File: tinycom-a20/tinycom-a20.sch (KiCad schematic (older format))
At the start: 36 parts, among them P1 CONN_02X08, P2 CONN_02X08, U1 ALLWINNERA10/TFBGA441, U2 H5TQG63BFR/FBGA96, U3 H27UBG8T2A/TSOP48, Y1 Crystal_Small, Y2 Crystal_Small

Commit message: add power routes
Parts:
- gave numbers to parts that had none: 2
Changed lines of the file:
@@
 $EndComp
 $Comp
-L GND #PWR01
+L GND #PWR21
 U 1 1 563E445F
 P 17800 6150
-F 0 "#PWR01" H 17800 5900 50  0001 C CNN
+F 0 "#PWR21" H 17800 5900 50  0001 C CNN
 F 1 "GND" H 17800 6000 50  0000 C CNN
 F 2 "" H 17800 6150 60  0000 C CNN
@@
 SCK_P
 $Comp
-L GND #PWR02
+L GND #PWR19
 U 1 1 563ECE56
 P 14950 850
-F 0 "#PWR02" H 14950 600 50  0001 C CNN
+F 0 "#PWR19" H 14950 600 50  0001 C CNN
 F 1 "GND" H 14950 700 50  0000 C CNN
 F 2 "" H 14950 850 60  0000 C CNN
@@
 $EndComp
 $Comp
-L GND #PWR03
+L GND #PWR17
 U 1 1 563EDF36
 P 13600 5900
-F 0 "#PWR03" H 13600 5650 50  0001 C CNN
+F 0 "#PWR17" H 13600 5650 50  0001 C CNN
 F 1 "GND" H 13600 5750 50  0000 C CNN
 F 2 "" H 13600 5900 60  0000 C CNN
@@
 $EndComp
 $Comp
-L GND #PWR04
+L GND #PWR18
 U 1 1 563EE398
 P 14350 5150
-F 0 "#PWR04" H 14350 4900 50  0001 C CNN
+F 0 "#PWR18" H 14350 4900 50  0001 C CNN
 F 1 "GND" H 14350 5000 50  0000 C CNN
 F 2 "" H 14350 5150 60  0000 C CNN
@@
 $EndComp
 $Comp
-L GND #PWR05
+L GND #PWR10
 U 1 1 56400687
 P 12400 9950
-F 0 "#PWR05" H 12400 9700 50  0001 C CNN
+F 0 "#PWR10" H 12400 9700 50  0001 C CNN
 F 1 "GND" H 12400 9800 50  0000 C CNN
 F 2 "" H 12400 9950 60  0000 C CNN
@@
 $EndComp
 $Comp
-L GND #PWR06
+L GND #PWR11
 U 1 1 56400704
 P 12650 9950
-F 0 "#PWR06" H 12650 9700 50  0001 C CNN
+F 0 "#PWR11" H 12650 9700 50  0001 C CNN
 F 1 "GND" H 12650 9800 50  0000 C CNN
 F 2 "" H 12650 9950 60  0000 C CNN
@@
 $EndComp
 $Comp
-L GND #PWR07
+L GND #PWR9
 U 1 1 56408532
 P 12150 9250
-F 0 "#PWR07" H 12150 9000 50  0001 C CNN
+F 0 "#PWR9" H 12150 9000 50  0001 C CNN
 F 1 "GND" H 12150 9100 50  0000 C CNN
 F 2 "" H 12150 9250 60  0000 C CNN
@@
 $EndComp
 $Comp
-L GND #PWR08
+L GND #PWR12
 U 1 1 56408573
 P 12700 9300
-F 0 "#PWR08" H 12700 9050 50  0001 C CNN
+F 0 "#PWR12" H 12700 9050 50  0001 C CNN
 F 1 "GND" H 12700 9150 50  0000 C CNN
 F 2 "" H 12700 9300 60  0000 C CNN
@@
 $EndComp
 $Comp
-L GND #PWR09
+L GND #PWR14
 U 1 1 5640D8CA
 P 12750 6950
-F 0 "#PWR09" H 12750 6700 50  0001 C CNN
+F 0 "#PWR14" H 12750 6700 50  0001 C CNN
 F 1 "GND" H 12750 6800 50  0000 C CNN
 F 2 "" H 12750 6950 60  0000 C CNN
@@
 $EndComp
 $Comp
-L GND #PWR010
+L GND #PWR24
 U 1 1 56408FCA
 P 19800 9350
-F 0 "#PWR010" H 19800 9100 50  0001 C CNN
+F 0 "#PWR24" H 19800 9100 50  0001 C CNN
 F 1 "GND" H 19800 9200 50  0000 C CNN
 F 2 "" H 19800 9350 60  0000 C CNN
@@
 UDP2
 $Comp
-L GND #PWR011
+L GND #PWR26
 U 1 1 56411561
 P 20650 10200
-F 0 "#PWR011" H 20650 9950 50  0001 C CNN
+F 0 "#PWR26" H 20650 9950 50  0001 C CNN
 F 1 "GND" H 20650 10050 50  0000 C CNN
 F 2 "" H 20650 10200 60  0000 C CNN
@@
 NoConn ~ 7500 2750
 $Comp
-L GND #PWR012
+L GND #PWR8
 U 1 1 56414A5D
 P 8850 1300
-F 0 "#PWR012" H 8850 1050 50  0001 C CNN
+F 0 "#PWR8" H 8850 1050 50  0001 C CNN
 F 1 "GND" H 8850 1150 50  0000 C CNN
 F 2 "" H 8850 1300 60  0000 C CNN
@@
 VCC_15
 $Comp
-L GND #PWR013
+L GND #PWR1
 U 1 1 56417328
 P 800 9350
-F 0 "#PWR013" H 800 9100 50  0001 C CNN
+F 0 "#PWR1" H 800 9100 50  0001 C CNN
 F 1 "GND" H 800 9200 50  0000 C CNN
 F 2 "" H 800 9350 60  0000 C CNN
@@
 NoConn ~ 1050 13300
 $Comp
-L GND #PWR014
+L GND #PWR3
 U 1 1 56417B02
 P 900 13450
-F 0 "#PWR014" H 900 13200 50  0001 C CNN
+F 0 "#PWR3" H 900 13200 50  0001 C CNN
 F 1 "GND" H 900 13300 50  0000 C CNN
 F 2 "" H 900 13450 60  0000 C CNN
@@
 NoConn ~ 1050 13700
 $Comp
-L GND #PWR015
+L GND #PWR2
 U 1 1 56417F5A
 P 850 13800
-F 0 "#PWR015" H 850 13550 50  0001 C CNN
+F 0 "#PWR2" H 850 13550 50  0001 C CNN
 F 1 "GND" H 850 13650 50  0000 C CNN
 F 2 "" H 850 13800 60  0000 C CNN
@@
 NoConn ~ 5650 11400
 $Comp
-L GND #PWR016
+L GND #PWR6
 U 1 1 56418E41
 P 5850 12050
-F 0 "#PWR016" H 5850 11800 50  0001 C CNN
+F 0 "#PWR6" H 5850 11800 50  0001 C CNN
 F 1 "GND" H 5850 11900 50  0000 C CNN
 F 2 "" H 5850 12050 60  0000 C CNN
@@
 $EndComp
 $Comp
-L GND #PWR017
+L GND #PWR7
 U 1 1 56419222
 P 5900 12300
-F 0 "#PWR017" H 5900 12050 50  0001 C CNN
+F 0 "#PWR7" H 5900 12050 50  0001 C CNN
 F 1 "GND" H 5900 12150 50  0000 C CNN
 F 2 "" H 5900 12300 60  0000 C CNN
@@
 NoConn ~ 11650 14450
 $Comp
-L GND #PWR018
+L GND #PWR16
 U 1 1 5641B53D
 P 12900 9850
-F 0 "#PWR018" H 12900 9600 50  0001 C CNN
+F 0 "#PWR16" H 12900 9600 50  0001 C CNN
 F 1 "GND" H 12900 9700 50  0000 C CNN
 F 2 "" H 12900 9850 60  0000 C CNN
@@
 NoConn ~ 13000 10700
 $Comp
-L GND #PWR019
+L GND #PWR15
 U 1 1 5641BA06
 P 12850 11350
-F 0 "#PWR019" H 12850 11100 50  0001 C CNN
+F 0 "#PWR15" H 12850 11100 50  0001 C CNN
 F 1 "GND" H 12850 11200 50  0000 C CNN
 F 2 "" H 12850 11350 60  0000 C CNN
@@
 NoConn ~ 13000 12600
 $Comp
-L GND #PWR020
+L GND #PWR13
 U 1 1 5641C0BF
 P 12700 12700
-F 0 "#PWR020" H 12700 12450 50  0001 C CNN
+F 0 "#PWR13" H 12700 12450 50  0001 C CNN
 F 1 "GND" H 12700 12550 50  0000 C CNN
 F 2 "" H 12700 12700 60  0000 C CNN
@@
 $EndComp
 $Comp
-L GND #PWR021
+L GND #PWR20
 U 1 1 5641C64B
 P 17750 14500
-F 0 "#PWR021" H 17750 14250 50  0001 C CNN
+F 0 "#PWR20" H 17750 14250 50  0001 C CNN
 F 1 "GND" H 17750 14350 50  0000 C CNN
 F 2 "" H 17750 14500 60  0000 C CNN
@@
 $EndComp
 $Comp
-L GND #PWR022
+L GND #PWR22
 U 1 1 5641CC6D
 P 17800 13850
-F 0 "#PWR022" H 17800 13600 50  0001 C CNN
+F 0 "#PWR22" H 17800 13600 50  0001 C CNN
 F 1 "GND" H 17800 13700 50  0000 C CNN
 F 2 "" H 17800 13850 60  0000 C CNN
@@
 VCC_33
 $Comp
-L GND #PWR023
+L GND #PWR27
 U 1 1 5643044F
 P 20800 13600
-F 0 "#PWR023" H 20800 13350 50  0001 C CNN
+F 0 "#PWR27" H 20800 13350 50  0001 C CNN
 F 1 "GND" H 20800 13450 50  0000 C CNN
 F 2 "" H 20800 13600 60  0000 C CNN
@@
 VCC_33
 $Comp
-L GND #PWR024
+L GND #PWR5
 U 1 1 5643A4FE
 P 5850 10900
-F 0 "#PWR024" H 5850 10650 50  0001 C CNN
+F 0 "#PWR5" H 5850 10650 50  0001 C CNN
 F 1 "GND" H 5850 10750 50  0000 C CNN
 F 2 "" H 5850 10900 60  0000 C CNN
@@
 NoConn ~ 1050 14100
 $Comp
-L GND #PWR025
+L GND #PWR4
 U 1 1 5643BDD7
 P 950 11000
-F 0 "#PWR025" H 950 10750 50  0001 C CNN
+F 0 "#PWR4" H 950 10750 50  0001 C CNN
 F 1 "GND" H 950 10850 50  0000 C CNN
 F 2 "" H 950 11000 60  0000 C CNN
@@
 VCC_33
 $Comp
-L GND #PWR026
+L GND #PWR23
 U 1 1 56440C85
 P 19500 8700
-F 0 "#PWR026" H 19500 8450 50  0001 C CNN
+F 0 "#PWR23" H 19500 8450 50  0001 C CNN
 F 1 "GND" H 19500 8550 50  0000 C CNN
 F 2 "" H 19500 8700 60  0000 C CNN
@@
 $EndComp
 $Comp
-L GND #PWR027
+L GND #PWR25
 U 1 1 56441E51
 P 20300 8700
-F 0 "#PWR027" H 20300 8450 50  0001 C CNN
+F 0 "#PWR25" H 20300 8450 50  0001 C CNN
 F 1 "GND" H 20300 8550 50  0000 C CNN
 F 2 "" H 20300 8700 60  0000 C CNN
@@
 $EndComp
 $Comp
-L GND #PWR028
+L GND #PWR28
 U 1 1 564426D1
 P 20950 8700
-F 0 "#PWR028" H 20950 8450 50  0001 C CNN
+F 0 "#PWR28" H 20950 8450 50  0001 C CNN
 F 1 "GND" H 20950 8550 50  0000 C CNN
 F 2 "" H 20950 8700 60  0000 C CNN
@@
 $EndComp
 $Comp
-L C_Small C?
+L C_Small C13
 U 1 1 5645F6BF
 P 21550 8450
-F 0 "C?" H 21560 8520 50  0000 L CNN
+F 0 "C13" H 21560 8520 50  0000 L CNN
 F 1 "C_Small" H 21560 8370 50  0000 L CNN
 F 2 "Capacitors_SMD:C_0603" H 21550 8450 60  0001 C CNN
@@
 $EndComp
 $Comp
-L C_Small C?
+L C_Small C18
 U 1 1 5645F746
 P 21650 8450
-F 0 "C?" H 21660 8520 50  0000 L CNN
+F 0 "C18" H 21660 8520 50  0000 L CNN
 F 1 "C_Small" H 21660 8370 50  0000 L CNN
 F 2 "Capacitors_SMD:C_0603" H 21650 8450 60  0001 C CNN

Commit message: fix
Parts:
- added C? (x2): C_Small, Capacitors_SMD:C_0603, symbol C_Small
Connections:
- net GND: now also C?.2, C?.2
- net VCC_12: now also C?.1
- net VCC_33: now also C?.1
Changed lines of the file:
@@
 	19900 8600 19900 8550
 Wire Wire Line
-	19050 8300 19500 8300
+	19050 8300 19650 8300
 Wire Wire Line
-	19050 8600 19500 8600
+	19050 8600 19650 8600
 Wire Wire Line
 	20700 8550 21650 8550
@@
 Connection ~ 21400 8550
 Connection ~ 21550 8550
+$Comp
+L C_Small C?
+U 1 1 5647248A
+P 20000 8450
+F 0 "C?" H 20010 8520 50  0000 L CNN
+F 1 "C_Small" H 20010 8370 50  0000 L CNN
+F 2 "Capacitors_SMD:C_0603" H 20000 8450 60  0001 C CNN
+F 3 "" H 20000 8450 60  0000 C CNN
+	1    20000 8450
+	1    0    0    -1
+$EndComp
+Wire Wire Line
+	20000 8350 20000 8300
+Connection ~ 20000 8300
+Wire Wire Line
+	20000 8550 20000 8600
+Connection ~ 20000 8600
+$Comp
+L C_Small C?
+U 1 1 56472991
+P 19650 8450
+F 0 "C?" H 19660 8520 50  0000 L CNN
+F 1 "C_Small" H 19660 8370 50  0000 L CNN
+F 2 "Capacitors_SMD:C_0603" H 19650 8450 60  0001 C CNN
+F 3 "" H 19650 8450 60  0000 C CNN
+	1    19650 8450
+	1    0    0    -1
+$EndComp
+Wire Wire Line
+	19650 8300 19650 8350
+Wire Wire Line
+	19650 8600 19650 8550
 $EndSCHEMATC

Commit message: readme
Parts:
- gave numbers to parts that had none: 2
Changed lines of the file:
@@
 $EndComp
 $Comp
-L GND #PWR21
+L GND #PWR01
 U 1 1 563E445F
 P 17800 6150
-F 0 "#PWR21" H 17800 5900 50  0001 C CNN
+F 0 "#PWR01" H 17800 5900 50  0001 C CNN
 F 1 "GND" H 17800 6000 50  0000 C CNN
 F 2 "" H 17800 6150 60  0000 C CNN
@@
 SCK_P
 $Comp
-L GND #PWR19
+L GND #PWR02
 U 1 1 563ECE56
 P 14950 850
-F 0 "#PWR19" H 14950 600 50  0001 C CNN
+F 0 "#PWR02" H 14950 600 50  0001 C CNN
 F 1 "GND" H 14950 700 50  0000 C CNN
 F 2 "" H 14950 850 60  0000 C CNN
@@
 $EndComp
 $Comp
-L GND #PWR17
+L GND #PWR03
 U 1 1 563EDF36
 P 13600 5900
-F 0 "#PWR17" H 13600 5650 50  0001 C CNN
+F 0 "#PWR03" H 13600 5650 50  0001 C CNN
 F 1 "GND" H 13600 5750 50  0000 C CNN
 F 2 "" H 13600 5900 60  0000 C CNN
@@
 $EndComp
 $Comp
-L GND #PWR18
+L GND #PWR04
 U 1 1 563EE398
 P 14350 5150
-F 0 "#PWR18" H 14350 4900 50  0001 C CNN
+F 0 "#PWR04" H 14350 4900 50  0001 C CNN
 F 1 "GND" H 14350 5000 50  0000 C CNN
 F 2 "" H 14350 5150 60  0000 C CNN
@@
 $EndComp
 $Comp
-L GND #PWR10
+L GND #PWR05
 U 1 1 56400687
 P 12400 9950
-F 0 "#PWR10" H 12400 9700 50  0001 C CNN
+F 0 "#PWR05" H 12400 9700 50  0001 C CNN
 F 1 "GND" H 12400 9800 50  0000 C CNN
 F 2 "" H 12400 9950 60  0000 C CNN
@@
 $EndComp
 $Comp
-L GND #PWR11
+L GND #PWR06
 U 1 1 56400704
 P 12650 9950
-F 0 "#PWR11" H 12650 9700 50  0001 C CNN
+F 0 "#PWR06" H 12650 9700 50  0001 C CNN
 F 1 "GND" H 12650 9800 50  0000 C CNN
 F 2 "" H 12650 9950 60  0000 C CNN
@@
 $EndComp
 $Comp
-L GND #PWR9
+L GND #PWR07
 U 1 1 56408532
 P 12150 9250
-F 0 "#PWR9" H 12150 9000 50  0001 C CNN
+F 0 "#PWR07" H 12150 9000 50  0001 C CNN
 F 1 "GND" H 12150 9100 50  0000 C CNN
 F 2 "" H 12150 9250 60  0000 C CNN
@@
 $EndComp
 $Comp
-L GND #PWR12
+L GND #PWR08
 U 1 1 56408573
 P 12700 9300
-F 0 "#PWR12" H 12700 9050 50  0001 C CNN
+F 0 "#PWR08" H 12700 9050 50  0001 C CNN
 F 1 "GND" H 12700 9150 50  0000 C CNN
 F 2 "" H 12700 9300 60  0000 C CNN
@@
 $EndComp
 $Comp
-L GND #PWR14
+L GND #PWR09
 U 1 1 5640D8CA
 P 12750 6950
-F 0 "#PWR14" H 12750 6700 50  0001 C CNN
+F 0 "#PWR09" H 12750 6700 50  0001 C CNN
 F 1 "GND" H 12750 6800 50  0000 C CNN
 F 2 "" H 12750 6950 60  0000 C CNN
@@
 $EndComp
 $Comp
-L GND #PWR24
+L GND #PWR010
 U 1 1 56408FCA
 P 19800 9350
-F 0 "#PWR24" H 19800 9100 50  0001 C CNN
+F 0 "#PWR010" H 19800 9100 50  0001 C CNN
 F 1 "GND" H 19800 9200 50  0000 C CNN
 F 2 "" H 19800 9350 60  0000 C CNN
@@
 UDP2
 $Comp
-L GND #PWR26
+L GND #PWR011
 U 1 1 56411561
 P 20650 10200
-F 0 "#PWR26" H 20650 9950 50  0001 C CNN
+F 0 "#PWR011" H 20650 9950 50  0001 C CNN
 F 1 "GND" H 20650 10050 50  0000 C CNN
 F 2 "" H 20650 10200 60  0000 C CNN
@@
 NoConn ~ 7500 2750
 $Comp
-L GND #PWR8
+L GND #PWR012
 U 1 1 56414A5D
 P 8850 1300
-F 0 "#PWR8" H 8850 1050 50  0001 C CNN
+F 0 "#PWR012" H 8850 1050 50  0001 C CNN
 F 1 "GND" H 8850 1150 50  0000 C CNN
 F 2 "" H 8850 1300 60  0000 C CNN
@@
 VCC_15
 $Comp
-L GND #PWR1
+L GND #PWR013
 U 1 1 56417328
 P 800 9350
-F 0 "#PWR1" H 800 9100 50  0001 C CNN
+F 0 "#PWR013" H 800 9100 50  0001 C CNN
 F 1 "GND" H 800 9200 50  0000 C CNN
 F 2 "" H 800 9350 60  0000 C CNN
@@
 NoConn ~ 1050 13300
 $Comp
-L GND #PWR3
+L GND #PWR014
 U 1 1 56417B02
 P 900 13450
-F 0 "#PWR3" H 900 13200 50  0001 C CNN
+F 0 "#PWR014" H 900 13200 50  0001 C CNN
 F 1 "GND" H 900 13300 50  0000 C CNN
 F 2 "" H 900 13450 60  0000 C CNN
@@
 NoConn ~ 1050 13700
 $Comp
-L GND #PWR2
+L GND #PWR015
 U 1 1 56417F5A
 P 850 13800
-F 0 "#PWR2" H 850 13550 50  0001 C CNN
+F 0 "#PWR015" H 850 13550 50  0001 C CNN
 F 1 "GND" H 850 13650 50  0000 C CNN
 F 2 "" H 850 13800 60  0000 C CNN
@@
 NoConn ~ 5650 11400
 $Comp
-L GND #PWR6
+L GND #PWR016
 U 1 1 56418E41
 P 5850 12050
-F 0 "#PWR6" H 5850 11800 50  0001 C CNN
+F 0 "#PWR016" H 5850 11800 50  0001 C CNN
 F 1 "GND" H 5850 11900 50  0000 C CNN
 F 2 "" H 5850 12050 60  0000 C CNN
@@
 $EndComp
 $Comp
-L GND #PWR7
+L GND #PWR017
 U 1 1 56419222
 P 5900 12300
-F 0 "#PWR7" H 5900 12050 50  0001 C CNN
+F 0 "#PWR017" H 5900 12050 50  0001 C CNN
 F 1 "GND" H 5900 12150 50  0000 C CNN
 F 2 "" H 5900 12300 60  0000 C CNN
@@
 NoConn ~ 11650 14450
 $Comp
-L GND #PWR16
+L GND #PWR018
 U 1 1 5641B53D
 P 12900 9850
-F 0 "#PWR16" H 12900 9600 50  0001 C CNN
+F 0 "#PWR018" H 12900 9600 50  0001 C CNN
 F 1 "GND" H 12900 9700 50  0000 C CNN
 F 2 "" H 12900 9850 60  0000 C CNN
@@
 NoConn ~ 13000 10700
 $Comp
-L GND #PWR15
+L GND #PWR019
 U 1 1 5641BA06
 P 12850 11350
-F 0 "#PWR15" H 12850 11100 50  0001 C CNN
+F 0 "#PWR019" H 12850 11100 50  0001 C CNN
 F 1 "GND" H 12850 11200 50  0000 C CNN
 F 2 "" H 12850 11350 60  0000 C CNN
@@
 NoConn ~ 13000 12600
 $Comp
-L GND #PWR13
+L GND #PWR020
 U 1 1 5641C0BF
 P 12700 12700
-F 0 "#PWR13" H 12700 12450 50  0001 C CNN
+F 0 "#PWR020" H 12700 12450 50  0001 C CNN
 F 1 "GND" H 12700 12550 50  0000 C CNN
 F 2 "" H 12700 12700 60  0000 C CNN
@@
 $EndComp
 $Comp
-L GND #PWR20
+L GND #PWR021
 U 1 1 5641C64B
 P 17750 14500
-F 0 "#PWR20" H 17750 14250 50  0001 C CNN
+F 0 "#PWR021" H 17750 14250 50  0001 C CNN
 F 1 "GND" H 17750 14350 50  0000 C CNN
 F 2 "" H 17750 14500 60  0000 C CNN
@@
 $EndComp
 $Comp
-L GND #PWR22
+L GND #PWR022
 U 1 1 5641CC6D
 P 17800 13850
-F 0 "#PWR22" H 17800 13600 50  0001 C CNN
+F 0 "#PWR022" H 17800 13600 50  0001 C CNN
 F 1 "GND" H 17800 13700 50  0000 C CNN
 F 2 "" H 17800 13850 60  0000 C CNN
@@
 VCC_33
 $Comp
-L GND #PWR27
+L GND #PWR023
 U 1 1 5643044F
 P 20800 13600
-F 0 "#PWR27" H 20800 13350 50  0001 C CNN
+F 0 "#PWR023" H 20800 13350 50  0001 C CNN
 F 1 "GND" H 20800 13450 50  0000 C CNN
 F 2 "" H 20800 13600 60  0000 C CNN
@@
 VCC_33
 $Comp
-L GND #PWR5
+L GND #PWR024
 U 1 1 5643A4FE
 P 5850 10900
-F 0 "#PWR5" H 5850 10650 50  0001 C CNN
+F 0 "#PWR024" H 5850 10650 50  0001 C CNN
 F 1 "GND" H 5850 10750 50  0000 C CNN
 F 2 "" H 5850 10900 60  0000 C CNN
@@
 NoConn ~ 1050 14100
 $Comp
-L GND #PWR4
+L GND #PWR025
 U 1 1 5643BDD7
 P 950 11000
-F 0 "#PWR4" H 950 10750 50  0001 C CNN
+F 0 "#PWR025" H 950 10750 50  0001 C CNN
 F 1 "GND" H 950 10850 50  0000 C CNN
 F 2 "" H 950 11000 60  0000 C CNN
@@
 VCC_33
 $Comp
-L GND #PWR23
+L GND #PWR026
 U 1 1 56440C85
 P 19500 8700
-F 0 "#PWR23" H 19500 8450 50  0001 C CNN
+F 0 "#PWR026" H 19500 8450 50  0001 C CNN
 F 1 "GND" H 19500 8550 50  0000 C CNN
 F 2 "" H 19500 8700 60  0000 C CNN
@@
 $EndComp
 $Comp
-L GND #PWR25
+L GND #PWR027
 U 1 1 56441E51
 P 20300 8700
-F 0 "#PWR25" H 20300 8450 50  0001 C CNN
+F 0 "#PWR027" H 20300 8450 50  0001 C CNN
 F 1 "GND" H 20300 8550 50  0000 C CNN
 F 2 "" H 20300 8700 60  0000 C CNN
@@
 $EndComp
 $Comp
-L GND #PWR28
+L GND #PWR028
 U 1 1 564426D1
 P 20950 8700
-F 0 "#PWR28" H 20950 8450 50  0001 C CNN
+F 0 "#PWR028" H 20950 8450 50  0001 C CNN
 F 1 "GND" H 20950 8550 50  0000 C CNN
 F 2 "" H 20950 8700 60  0000 C CNN
@@
 Connection ~ 21550 8550
 $Comp
-L C_Small C?
+L C_Small C22
 U 1 1 5647248A
 P 20000 8450
-F 0 "C?" H 20010 8520 50  0000 L CNN
+F 0 "C22" H 20010 8520 50  0000 L CNN
 F 1 "C_Small" H 20010 8370 50  0000 L CNN
 F 2 "Capacitors_SMD:C_0603" H 20000 8450 60  0001 C CNN
@@
 Connection ~ 20000 8600
 $Comp
-L C_Small C?
+L C_Small C21
 U 1 1 56472991
 P 19650 8450
-F 0 "C?" H 19660 8520 50  0000 L CNN
+F 0 "C21" H 19660 8520 50  0000 L CNN
 F 1 "C_Small" H 19660 8370 50  0000 L CNN
 F 2 "Capacitors_SMD:C_0603" H 19650 8450 60  0001 C CNN

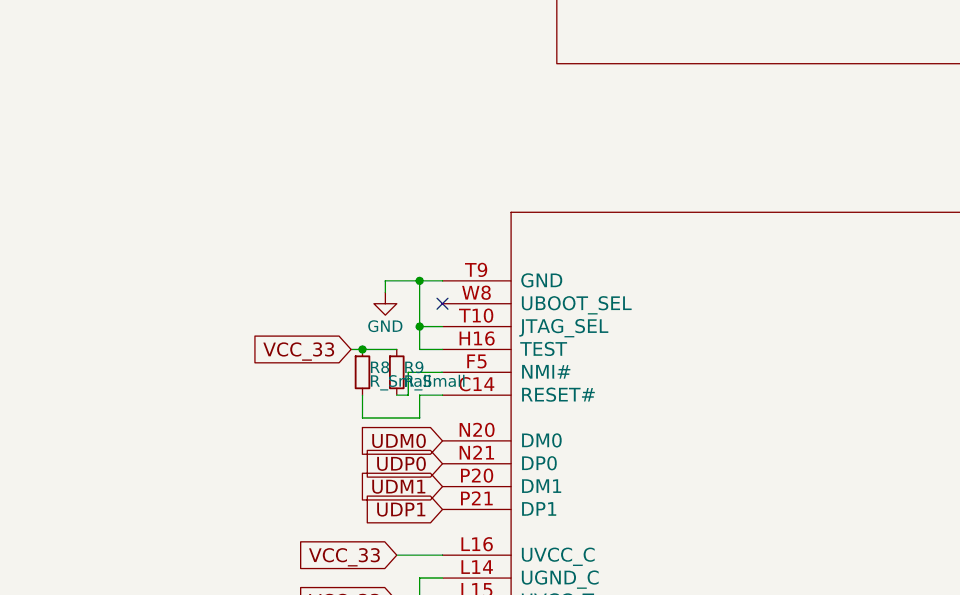
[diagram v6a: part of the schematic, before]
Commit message: add uboot_sel test point
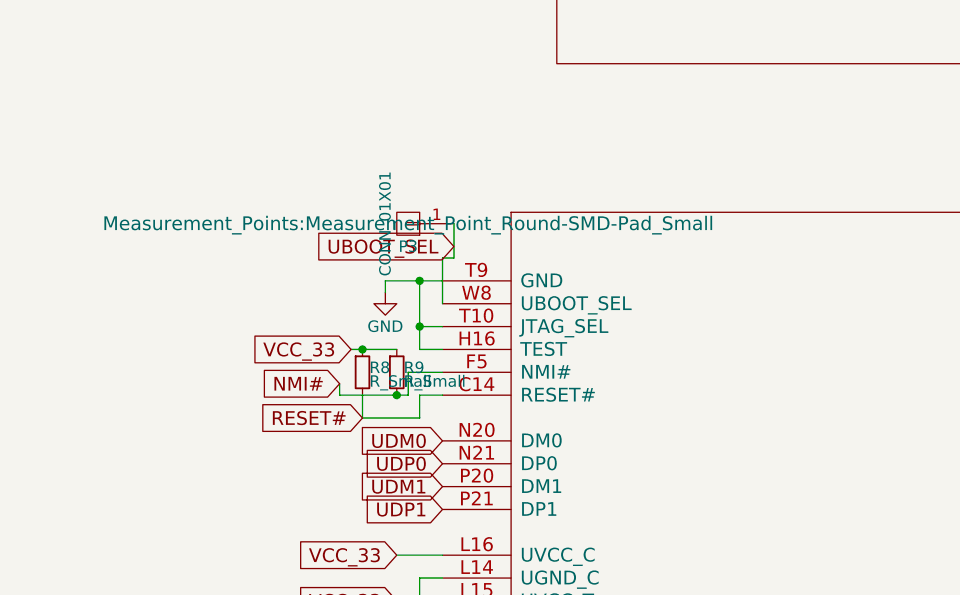
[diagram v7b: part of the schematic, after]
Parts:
- added P3: CONN_01X01, Measurement_Points:Measurement_Point_Round-SMD-Pad_Small, symbol CONN_01X01
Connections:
- net RESET#: now reaches R8.2, U1.C14 (RESET#)
- net NMI#: now reaches R9.2, U1.F5 (NMI#)
- net UBOOT_SEL: now reaches U1.W8 (UBOOT_SEL)
- net UBOOT_SEL: now also P3.1 (P1)
- no-connect marks 233 -> 232
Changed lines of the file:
@@
 Text GLabel 850  10900 0    60   Input ~ 0
 VCC_12
-NoConn ~ 1050 9400
 Text GLabel 650  9600 0    60   Input ~ 0
 VCC_33
@@
 	1050 9700 900  9700
 Wire Wire Line
-	900  9700 900  9800
-Wire Wire Line
-	900  9800 850  9800
+	900  9800 900  9700
+Wire Wire Line
+	600  9800 900  9800
 Wire Wire Line
 	650  9600 850  9600
@@
 Wire Wire Line
 	19650 8600 19650 8550
+Wire Wire Line
+	1050 9400 1050 9200
+Wire Wire Line
+	1050 9200 1100 9200
+Wire Wire Line
+	1100 9200 1100 9050
+$Comp
+L CONN_01X01 P3
+U 1 1 56507657
+P 900 9050
+F 0 "P3" H 900 9150 50  0000 C CNN
+F 1 "CONN_01X01" V 1000 9050 50  0000 C CNN
+F 2 "Measurement_Points:Measurement_Point_Round-SMD-Pad_Small" H 900 9050 60  0000 C CNN
+F 3 "" H 900 9050 60  0000 C CNN
+	1    900  9050
+	-1   0    0    1
+$EndComp
+Text GLabel 1100 9150 0    60   Input ~ 0
+UBOOT_SEL
+Text GLabel 700  9900 0    60   Input ~ 0
+RESET#
+Text GLabel 600  9750 0    60   Input ~ 0
+NMI#
+Wire Wire Line
+	600  9800 600  9750
+Connection ~ 850  9800
 $EndSCHEMATC

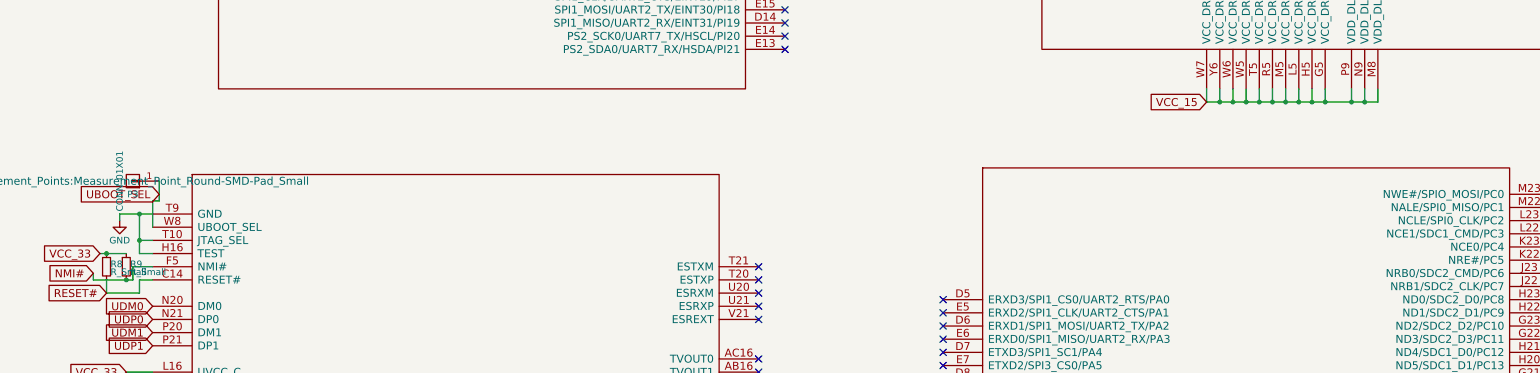
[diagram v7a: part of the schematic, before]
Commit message: fix vcc_dll
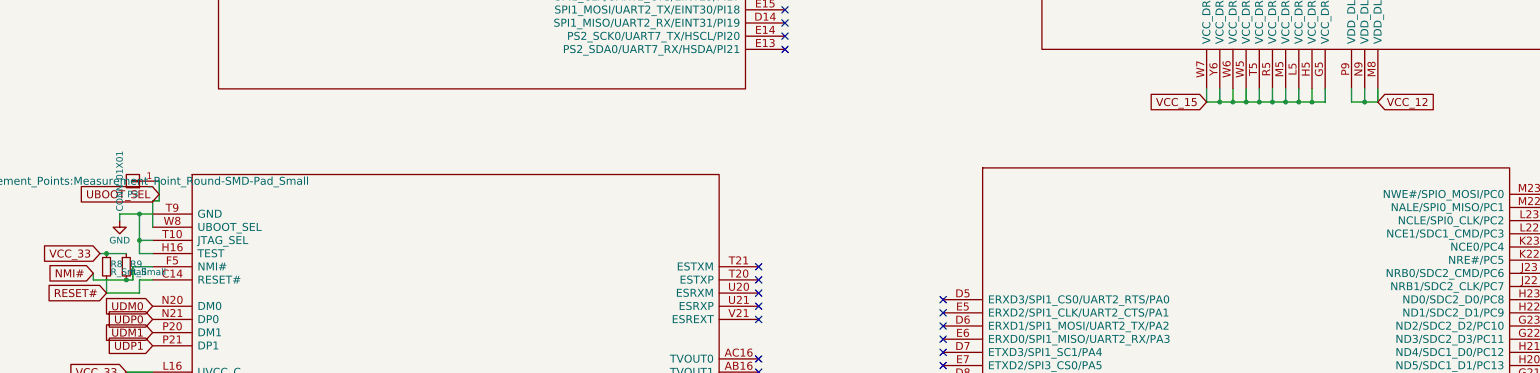
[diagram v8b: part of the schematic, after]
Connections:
- net VCC_12: now also U1.M8 (VDD_DLL), U1.N9 (VDD_DLL), U1.P9 (VDD_DLL)
- net VCC_15: no longer U1.M8 (VDD_DLL), U1.N9 (VDD_DLL), U1.P9 (VDD_DLL)
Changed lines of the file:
@@
 	9050 8350 9050 8450
-Wire Wire Line
-	9050 8450 10350 8450
 Wire Wire Line
 	10350 8450 10350 8350
@@
 Wire Wire Line
 	9950 8350 9950 8450
-Connection ~ 9950 8450
 Wire Wire Line
 	10150 8350 10150 8450
-Connection ~ 10150 8450
 Wire Wire Line
 	10250 8350 10250 8450
@@
 	1050 9700 900  9700
 Wire Wire Line
-	900  9800 900  9700
-Wire Wire Line
-	600  9800 900  9800
+	900  9700 900  9800
+Wire Wire Line
+	900  9800 600  9800
 Wire Wire Line
 	650  9600 850  9600
@@
 	600  9800 600  9750
 Connection ~ 850  9800
+Wire Wire Line
+	9950 8450 9050 8450
+Wire Wire Line
+	10150 8450 10350 8450
+Text GLabel 10350 8450 2    60   Input ~ 0
+VCC_12
 $EndSCHEMATC
